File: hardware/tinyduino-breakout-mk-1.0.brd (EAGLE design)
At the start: 20 x 20 mm, 4 parts, among them J1 DF12-32-DP

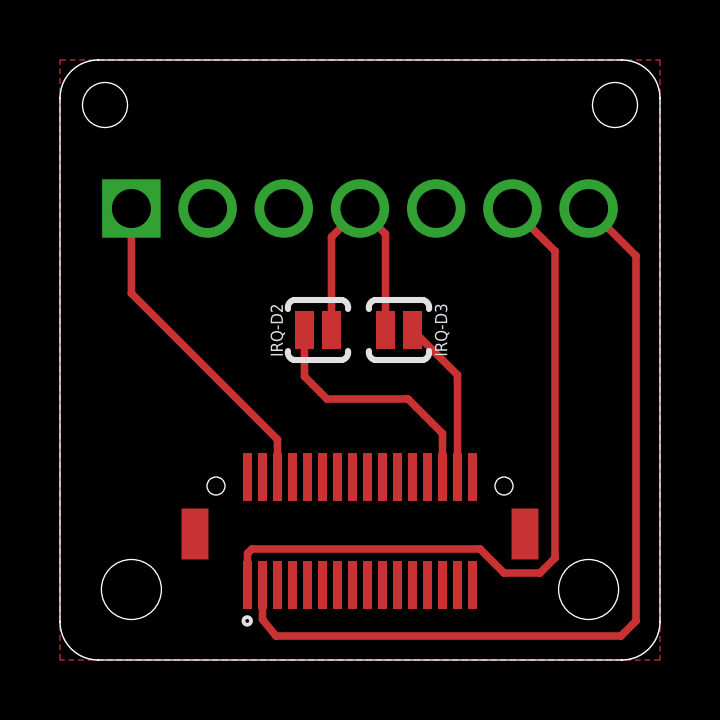
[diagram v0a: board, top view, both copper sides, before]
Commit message: adding revsion info to schematic and board
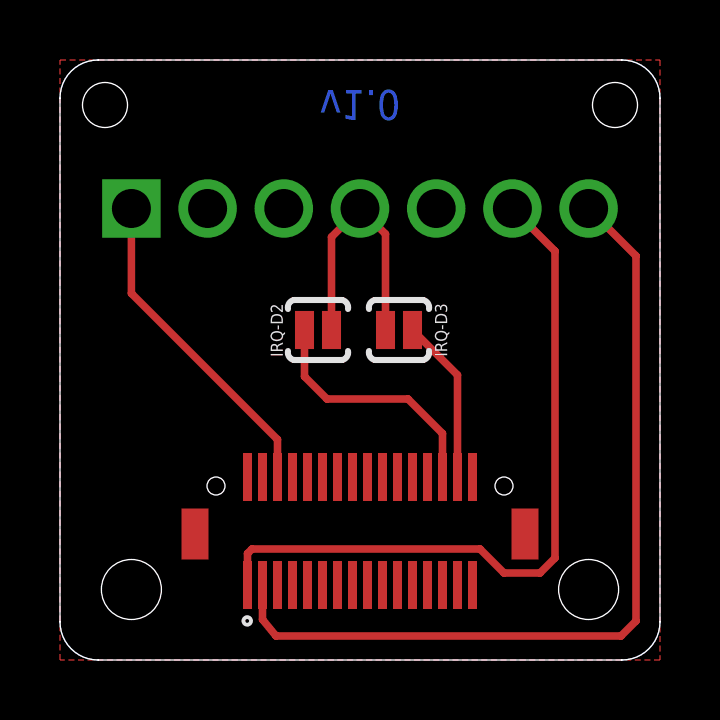
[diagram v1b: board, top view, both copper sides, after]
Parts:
- added FRAME1: FRAME-LETTERNO_PACKAGE, A_butts:DUMMY
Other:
- board text added: ">VERSION"
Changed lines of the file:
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@@
 <setting verticaltext="up"/>
 </settings>
-<grid distance="0.1" unitdist="mm" unit="mm" style="lines" multiple="1" display="yes" altdistance="1" altunitdist="inch" altunit="inch"/>
+<grid distance="0.5" unitdist="mm" unit="mm" style="lines" multiple="2" display="yes" altdistance="1" altunitdist="mil" altunit="mil"/>
 <layers>
 <layer number="1" name="Top" color="4" fill="1" visible="yes" active="yes"/>
@@
 <layer number="56" name="wert" color="7" fill="1" visible="no" active="no"/>
 <layer number="57" name="tCAD" color="7" fill="1" visible="no" active="no"/>
+<layer number="90" name="Modules" color="5" fill="1" visible="yes" active="yes"/>
 <layer number="91" name="Nets" color="2" fill="1" visible="no" active="no"/>
 <layer number="92" name="Busses" color="1" fill="1" visible="no" active="no"/>
@@
 <layer number="223" name="223bmp" color="24" fill="1" visible="yes" active="yes"/>
 <layer number="224" name="224bmp" color="25" fill="1" visible="yes" active="yes"/>
+<layer number="225" name="225bmp" color="7" fill="1" visible="yes" active="yes"/>
+<layer number="226" name="226bmp" color="7" fill="1" visible="yes" active="yes"/>
+<layer number="227" name="227bmp" color="7" fill="1" visible="yes" active="yes"/>
+<layer number="228" name="228bmp" color="7" fill="1" visible="yes" active="yes"/>
+<layer number="229" name="229bmp" color="7" fill="1" visible="yes" active="yes"/>
+<layer number="230" name="230bmp" color="7" fill="1" visible="yes" active="yes"/>
+<layer number="231" name="231bmp" color="7" fill="1" visible="yes" active="yes"/>
 <layer number="248" name="Housing" color="7" fill="1" visible="yes" active="yes"/>
 <layer number="249" name="Edge" color="7" fill="1" visible="yes" active="yes"/>
@@
 <text x="10" y="12.3" size="0.6096" layer="22" font="vector" ratio="12" rot="SMR180" align="bottom-center">Sensor This Side
 (face up, in case that wasn't obvious)</text>
+<text x="10" y="18.5" size="1" layer="16" font="vector" ratio="16" rot="SMR180" align="center">&gt;VERSION</text>
+<text x="10" y="18.5" size="1" layer="22" font="vector" ratio="16" rot="SMR180" align="center">&gt;VERSION</text>
 </plain>
 <attributes>
+<attribute name="VERSION" value="v1.0"/>
 </attributes>
 <variantdefs>
@@
 </element>
 <element name="BRK1" library="A_butts" package="ADAFRUIT-SI1145-BREAKOUT" value="ADAFRUIT-SI1145-BREAKOUT" x="10" y="8.7" rot="MR180"/>
+<element name="FRAME1" library="A_butts" package="DUMMY" value="FRAME-LETTERNO_PACKAGE" x="0" y="-0.5">
+<attribute name="VERSION" value="v1.0" x="0" y="-0.5" size="0.5" layer="27" ratio="12" display="off"/>
+<attribute name="DESIGNER" value="sean@yak.net" x="0" y="-0.5" size="0.5" layer="27" ratio="12" display="off"/>
+</element>
 </elements>
 <signals>
